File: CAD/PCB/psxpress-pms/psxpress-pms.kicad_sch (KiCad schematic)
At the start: 18 parts, among them IC1 BQ25606RGER

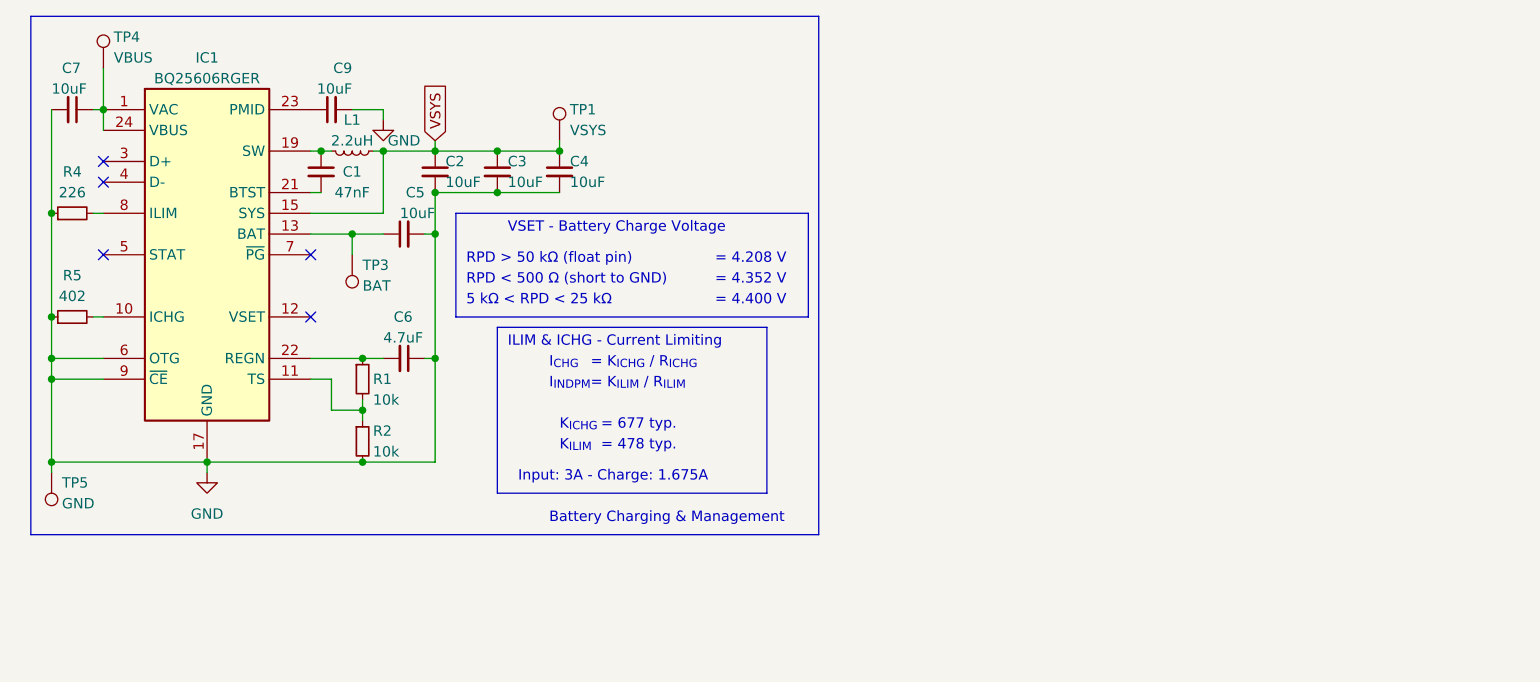
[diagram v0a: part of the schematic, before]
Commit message: pms - finish battery management circuit & add soft power switch circuit
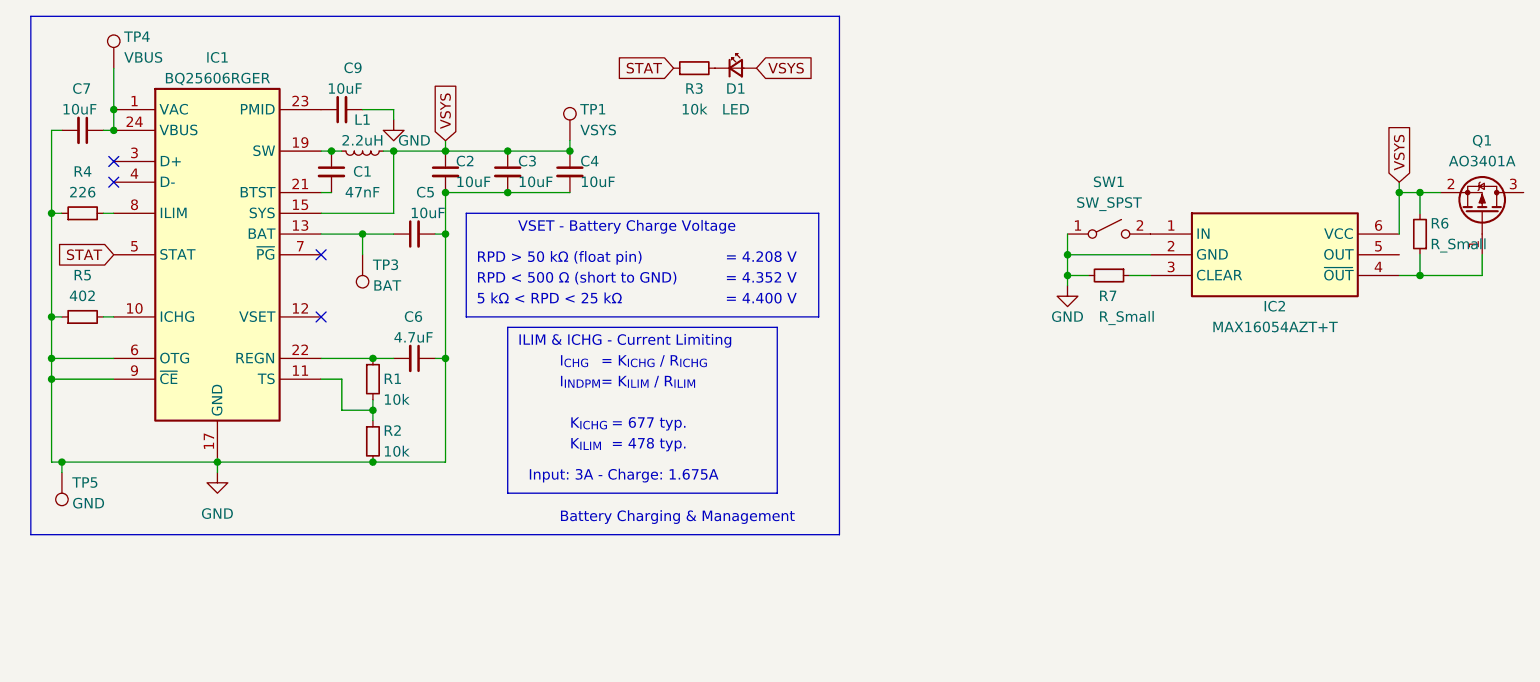
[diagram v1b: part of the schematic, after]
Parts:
- added D1: LED, symbol Device:LED_Small
- added IC2: MAX16054AZT+T, SOT95P275X110-6N, symbol MAX16054AZT+T:MAX16054AZT+T
- added Q1: AO3401A, Package_TO_SOT_SMD:SOT-23, symbol Transistor_FET:AO3401A
- added R3: 10k, symbol Device:R_Small
- added R6, R7: R_Small, symbol Device:R_Small
- added SW1: SW_SPST, symbol Switch:SW_SPST
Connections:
- net GND: now also IC2.2 (GND), R7.2, SW1.1 (A)
- net VSYS: now also D1.2 (A), IC2.6 (VCC), Q1.2 (S), R6.2
- net STAT: now reaches IC1.5 (STAT)
- net STAT: now also R3.1
- new net: IC2.4 (~{OUT}), Q1.1 (G), R6.1
- new net: D1.1 (K), R3.2
- new net: IC2.3 (CLEAR), R7.1
- new net: IC2.1 (IN), SW1.2 (B)
- no-connect marks 5 -> 4
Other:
- moved on the sheet: C1, C2, C3, C4, C5, C6, C7, C9, IC1, L1, R1, R2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

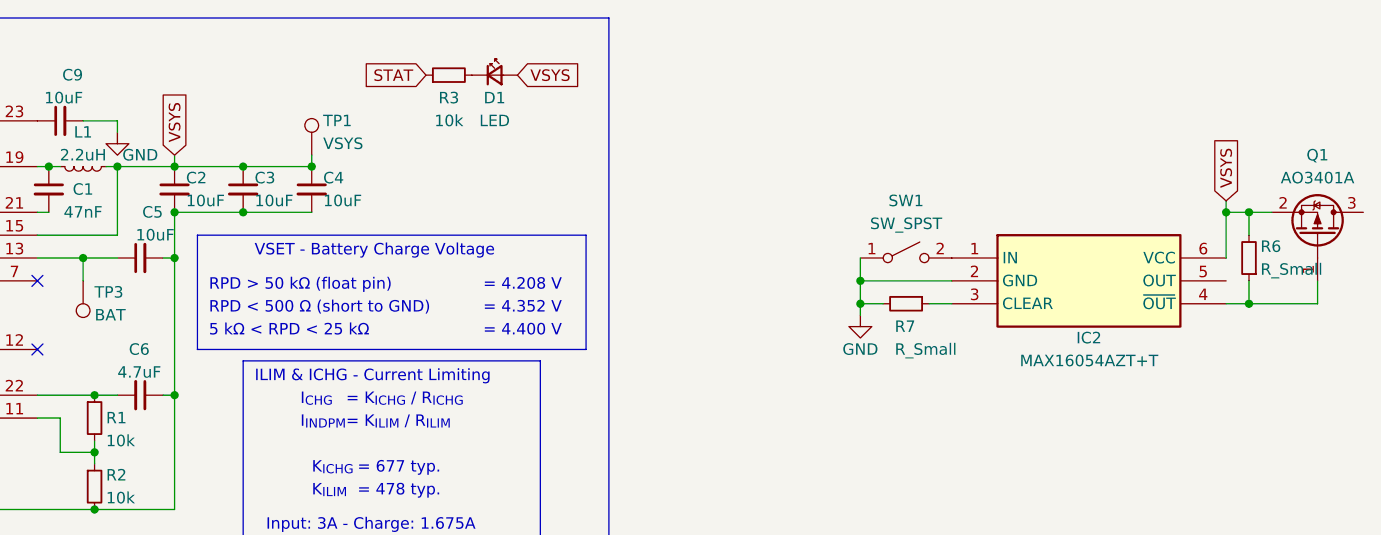
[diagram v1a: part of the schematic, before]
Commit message: pms - actually add the soft power switch circuit this time -.-
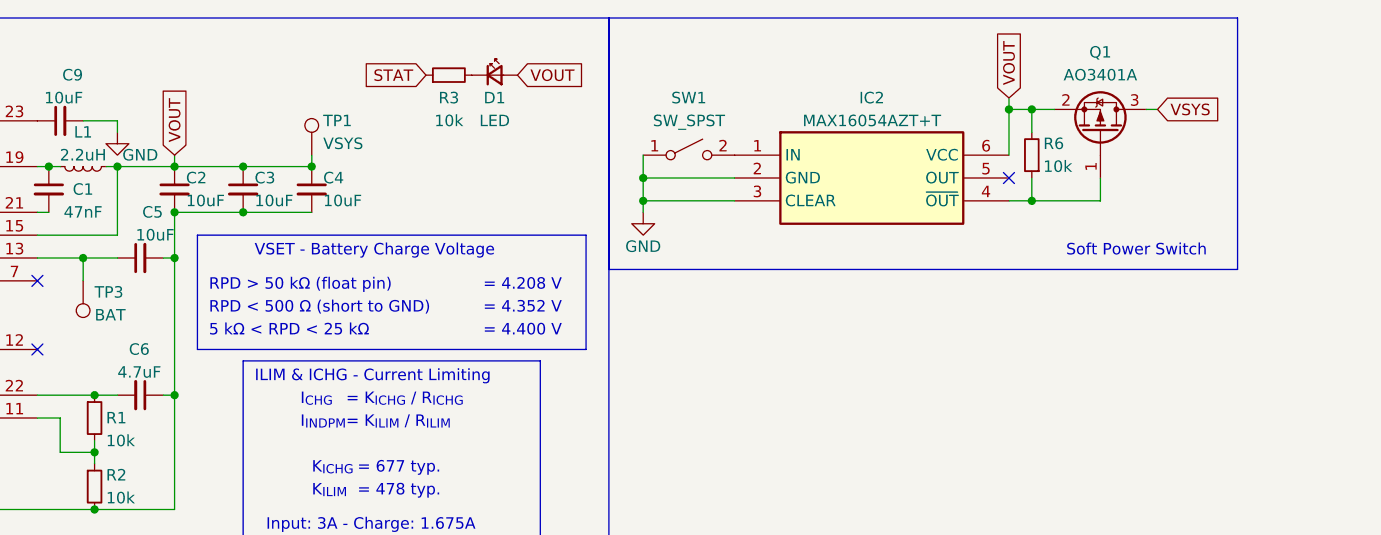
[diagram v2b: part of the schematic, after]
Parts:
- removed R7: R_Small, symbol Device:R_Small
- R6: value R_Small -> 10k
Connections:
- net GND: now also IC2.3 (CLEAR)
- net VSYS: now also Q1.3 (D); no longer C2.1, C3.1, C4.1, D1.2 (A), IC1.15 (SYS), IC1.16 (SYS), IC2.6 (VCC), L1.1, Q1.2 (S), R6.2, TP1.1
- new net VOUT: C2.1, C3.1, C4.1, D1.2 (A), IC1.15 (SYS), IC1.16 (SYS), IC2.6 (VCC), L1.1, Q1.2 (S), R6.2, TP1.1
- no-connect marks 4 -> 5
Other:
- note added: "Soft Power Switch"
- moved on the sheet: IC2, Q1, R6, SW1

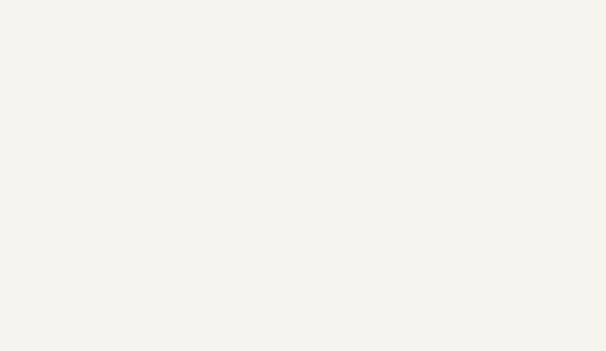
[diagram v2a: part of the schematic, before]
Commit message: pms - add logo & design info to schematic
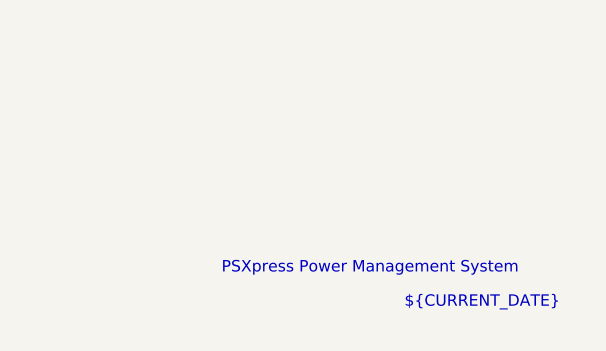
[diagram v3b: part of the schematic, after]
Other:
- note added: "${CURRENT_DATE}"
- note added: "PSXpress Power Management System"

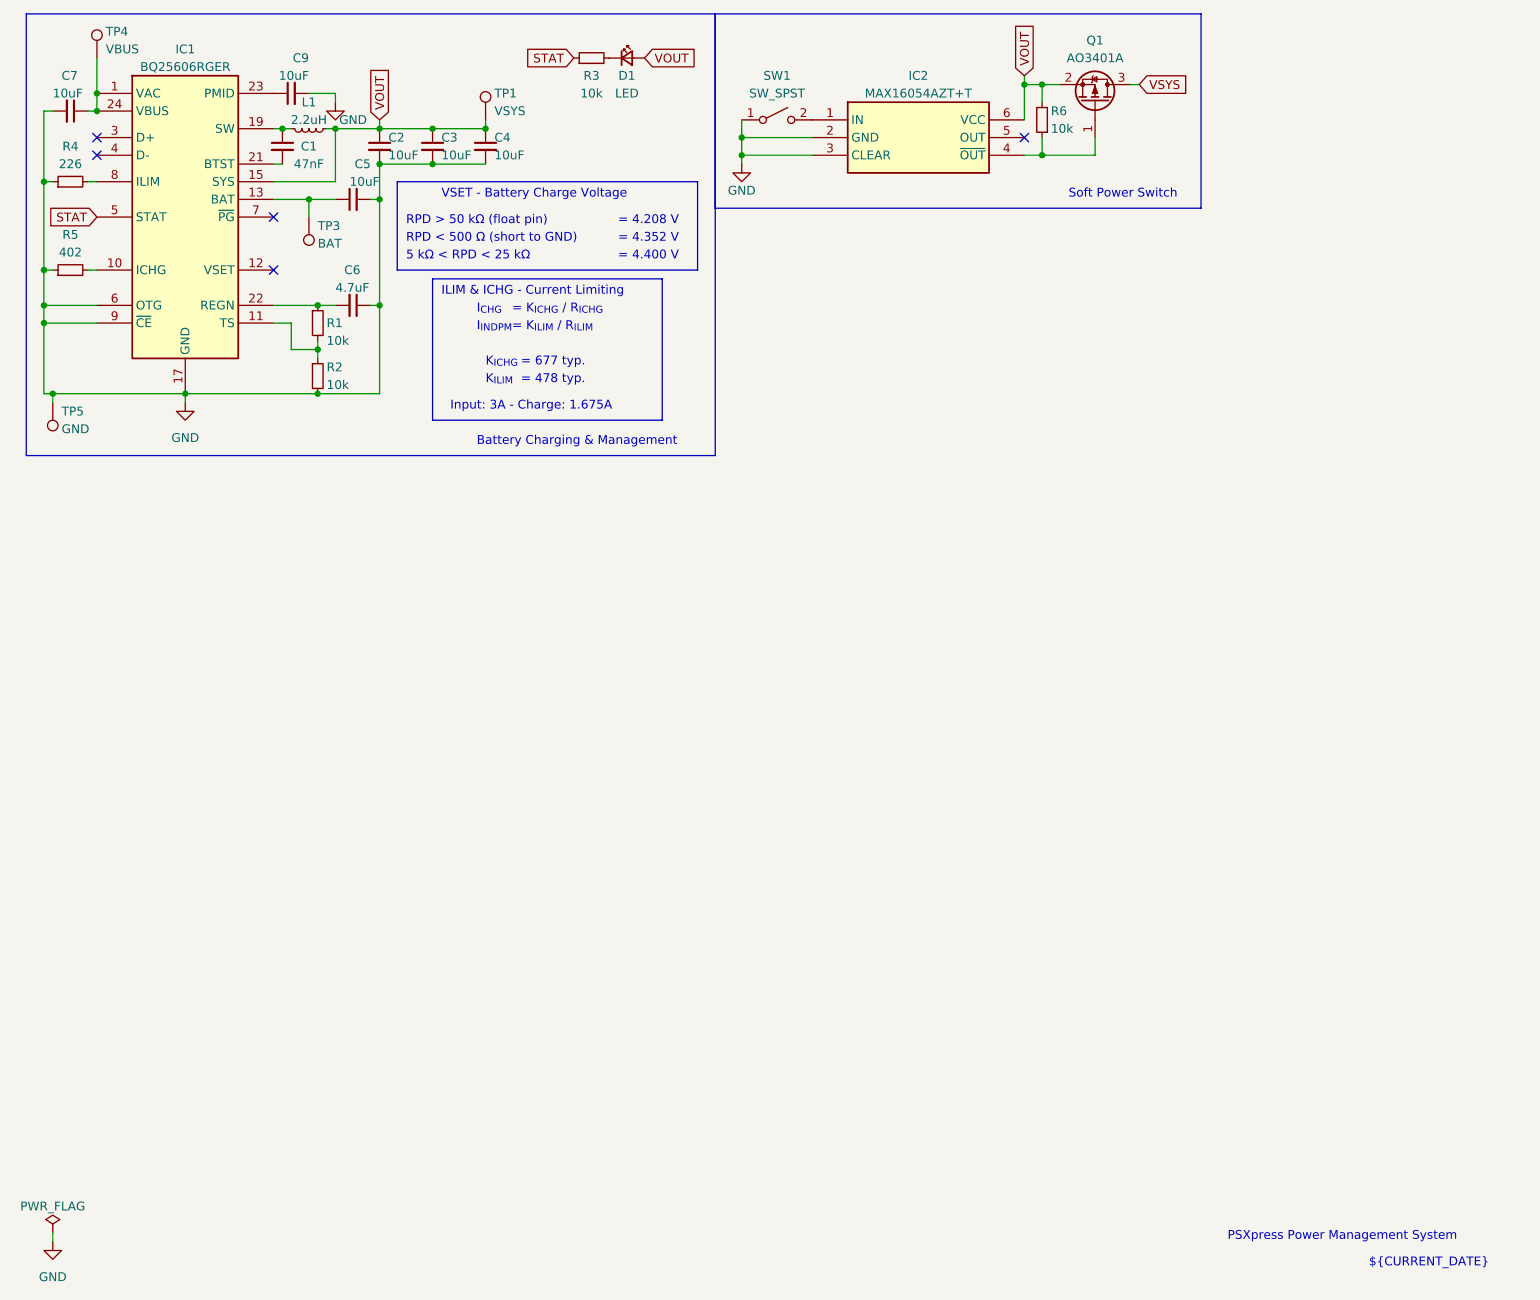
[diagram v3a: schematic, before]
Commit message: pms - add dcdc regulator circuits & tidy schematic
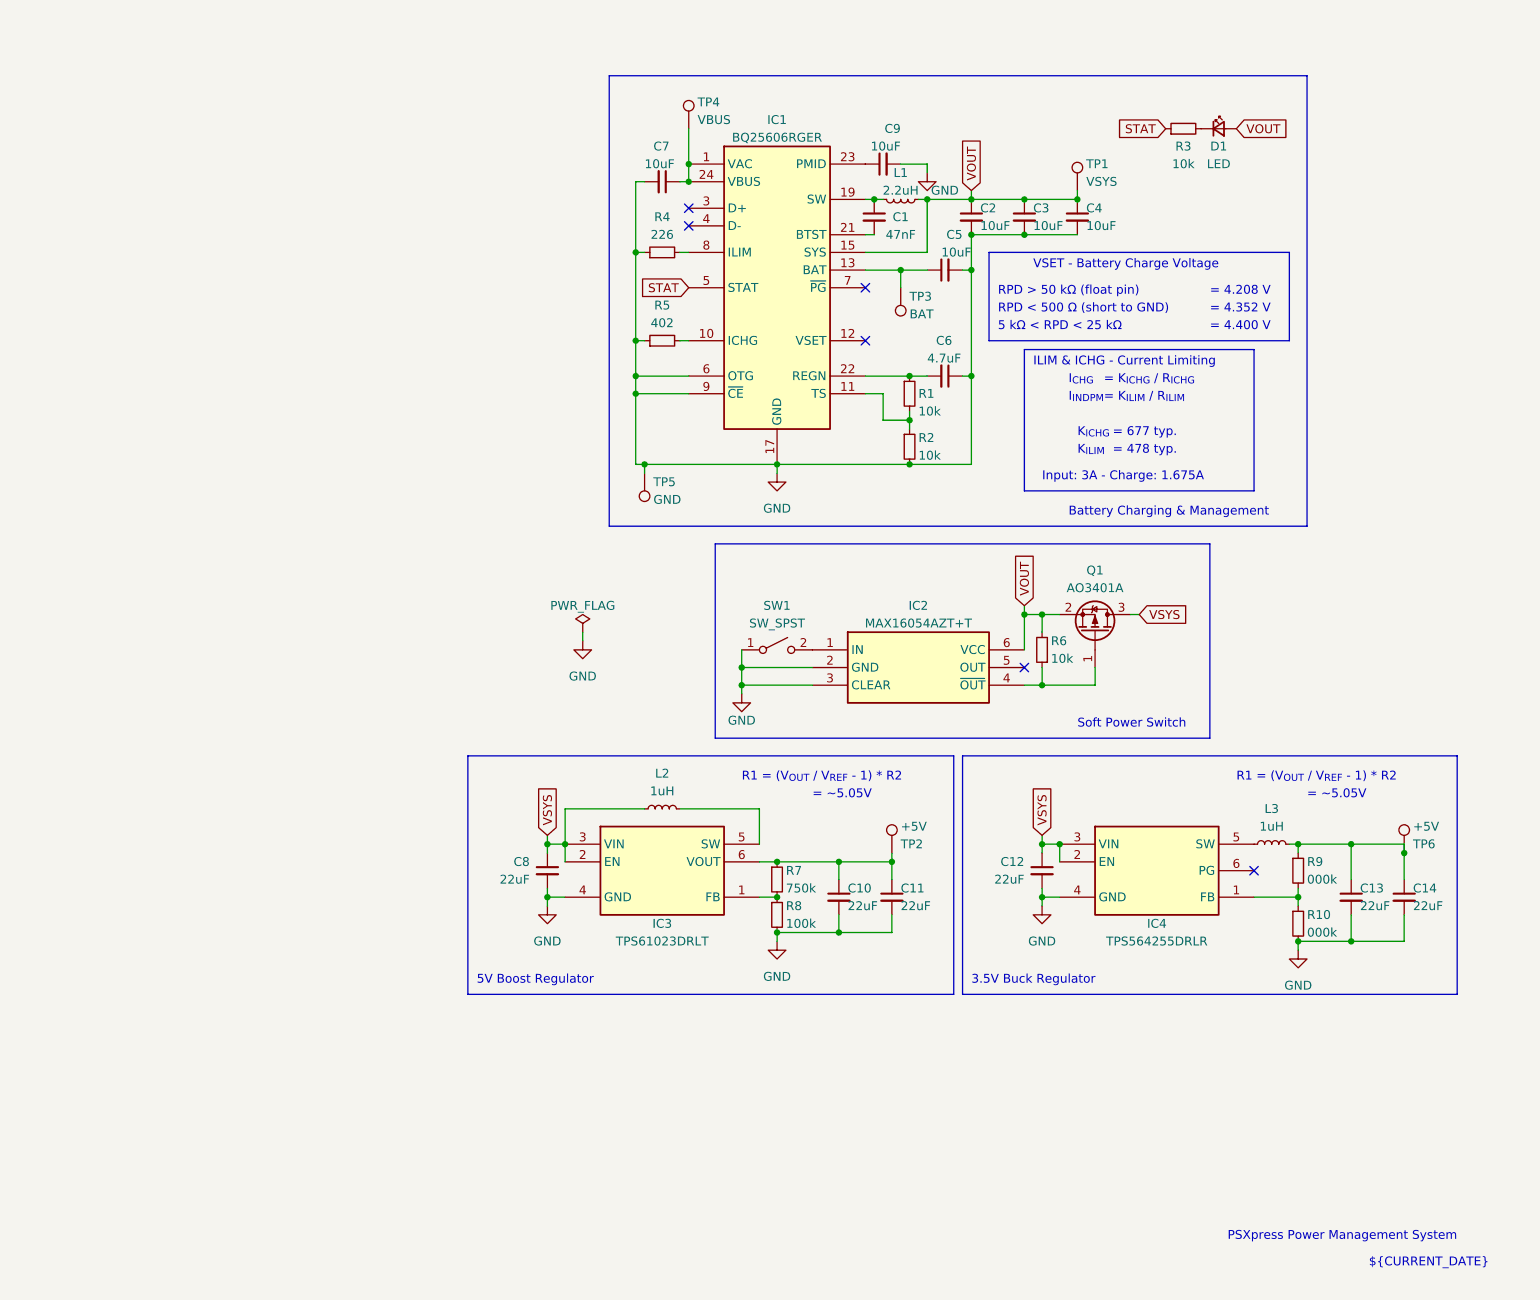
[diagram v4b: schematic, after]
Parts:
- added C10, C11, C12, C13, C14, C8: 22uF, symbol Device:C_Small
- added IC3: TPS61023DRLT, SOTFL50P160X60-6N, symbol TPS61023DRLT:TPS61023DRLT
- added IC4: TPS564255DRLR, SOTFL50P160X60-6N, symbol TPS564255DRLR:TPS564255DRLR
- added L2, L3: 1uH, symbol Device:L_Small
- added R10, R9: 000k, symbol Device:R_Small
- added R7: 750k, symbol Device:R_Small
- added R8: 100k, symbol Device:R_Small
- added TP2, TP6: +5V, symbol Connector:TestPoint
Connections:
- net GND: now also C10.2, C11.2, C12.2, C13.2, C14.2, C8.2, IC3.4 (GND), IC4.4 (GND), R10.2, R8.2
- net VSYS: now also C12.1, C8.1, IC3.2 (EN), IC3.3 (VIN), IC4.2 (EN), IC4.3 (VIN), L2.1
- new net: C13.1, C14.1, L3.2, R9.1, TP6.1
- new net: C10.1, C11.1, IC3.6 (VOUT), R7.1, TP2.1
- new net: IC3.1 (FB), R7.2, R8.1
- new net: IC4.1 (FB), R10.1, R9.2
- new net: IC3.5 (SW), L2.2
- new net: IC4.5 (SW), L3.1
- no-connect marks 5 -> 6
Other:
- note added: "3.5V Buck Regulator"
- note added: "5V Boost Regulator"
- note added: "= ~5.05V"
- note added: "R1 = (V_{OUT} / V_{REF} - 1) * R2"
- moved on the sheet: C1, C2, C3, C4, C5, C6, C7, C9, D1, IC1, IC2, L1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

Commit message: pms - forgot to save again
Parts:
- R10: value 000k -> 100k
- R9: value 000k -> 487k
- TP6: value +5V -> +3V5
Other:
- note added: "= ~3.52V"
- note added: "R7 = (V_{OUT} / V_{REF} - 1) * R8"
- note added: "V_{OUT} = 0.6 * (1 + R9 / R10)"
- note removed: "R1 = (V_{OUT} / V_{REF} - 1) * R2"
- moved on the sheet: C12, C13, C14, IC4, L3, R10, R9, TP6
